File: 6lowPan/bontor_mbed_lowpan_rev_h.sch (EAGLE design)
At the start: 173 parts, among them IC1 SIM900, IC2 74HC595D, IC3 74HC595D, IC4 ADE7758RW, IC5 74HC595D, U2 W5500, X1 NX2520SA

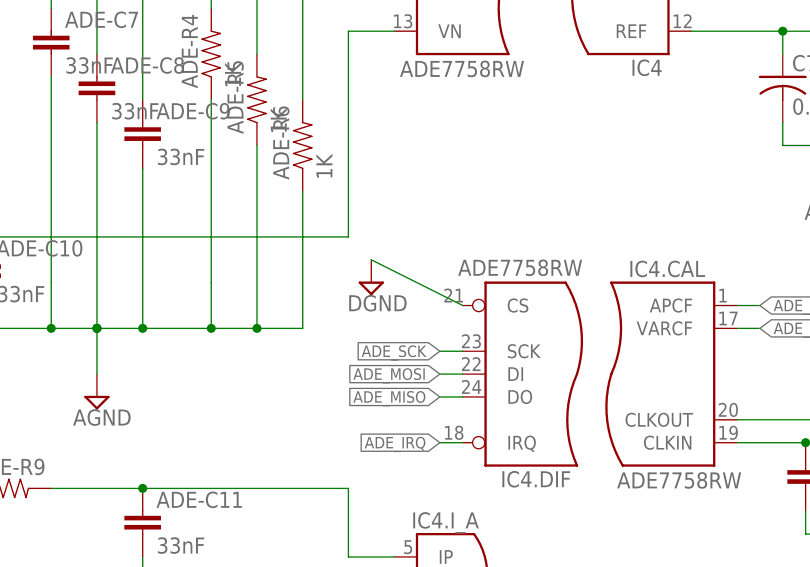
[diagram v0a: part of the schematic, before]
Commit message: add mcb enhancer BoM and gerber
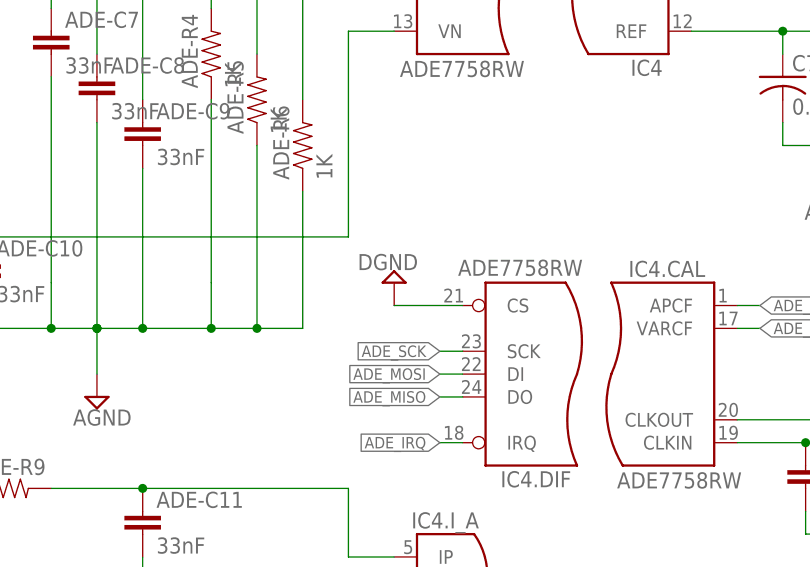
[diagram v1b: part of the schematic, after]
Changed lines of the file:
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@@
 <instance part="SUPPLY121" gate="G$1" x="622.3" y="119.38"/>
 <instance part="SUPPLY122" gate="G$1" x="546.1" y="25.4"/>
-<instance part="SUPPLY123" gate="G$1" x="299.72" y="144.78"/>
+<instance part="SUPPLY123" gate="G$1" x="302.26" y="144.78" rot="R180"/>
 <instance part="SUPPLY124" gate="G$1" x="502.92" y="106.68"/>
 <instance part="L1" gate="L" x="347.98" y="38.1" rot="R90"/>
@@
 <segment>
 <pinref part="IC4" gate=".DIF" pin="CS"/>
-<wire x1="309.88" y1="142.24" x2="299.72" y2="147.32" width="0.2032" layer="91"/>
+<wire x1="309.88" y1="142.24" x2="302.26" y2="142.24" width="0.2032" layer="91"/>
 <pinref part="SUPPLY123" gate="G$1" pin="DGND"/>
 </segment>

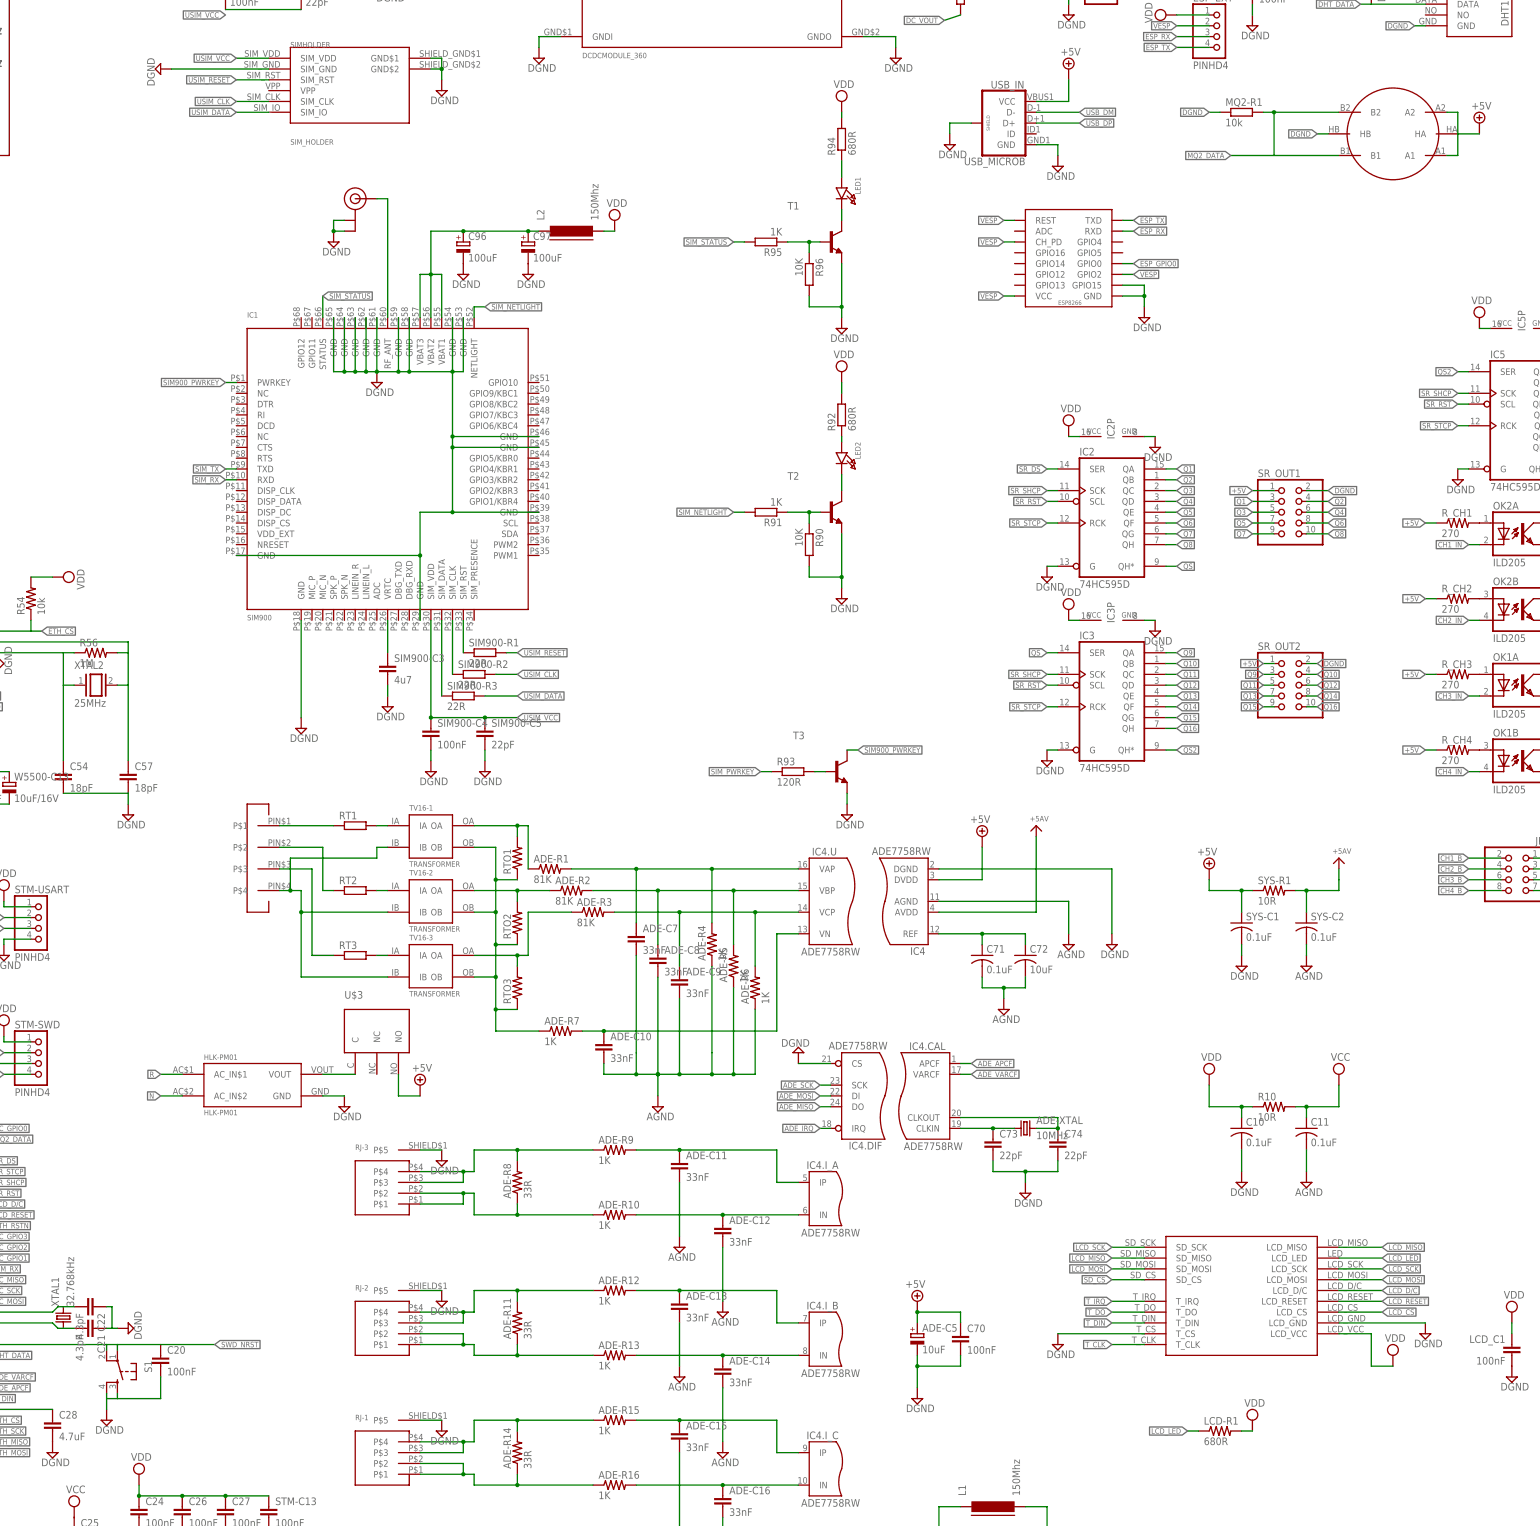
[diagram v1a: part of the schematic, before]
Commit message: added on off button and remove LCD resstor
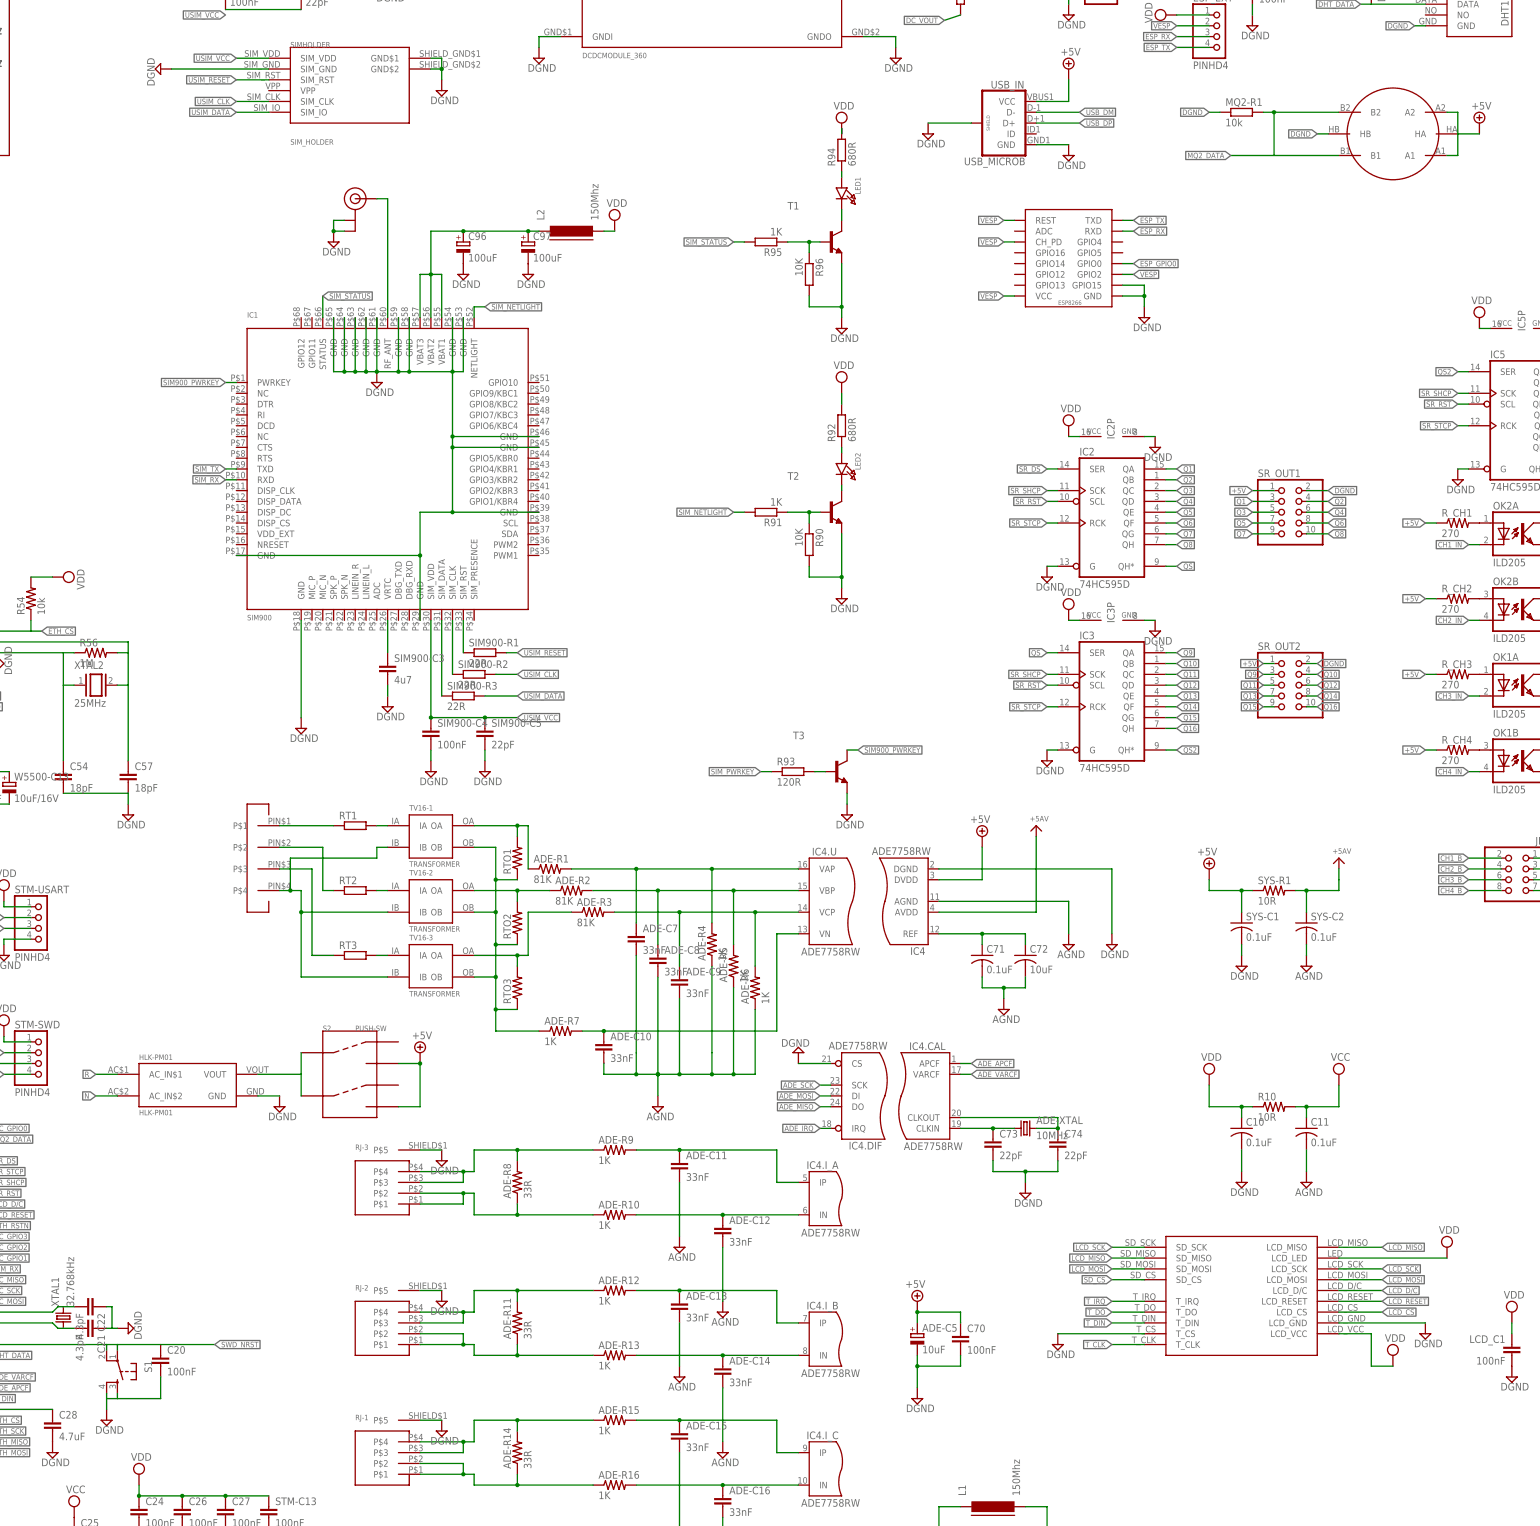
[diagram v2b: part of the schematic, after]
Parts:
- removed LCD-R1: 680R, SparkFun-Passives:RESISTOR0603-RES
- removed U$3: SW-KN1-102, bontor:SW-KN1-102
- added S2: PUSH-SW, Itead_BP_110825:SWITCH-6PIN-LOCK-2.54MM
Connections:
- removed net LCD_LED: LCD-R1.1, LCD14.LCD_LED
- net +5V: now also S2.P$3, S2.P$6; no longer U$3.NO
- net N$79: now also S2.P$1, S2.P$4; no longer U$3.C
- net VDD: now also LCD14.LCD_LED; no longer LCD-R1.2
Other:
- moved on the sheet: HLK-PM01, LED2, R92, R94
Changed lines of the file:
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@@
 <?xml version="1.0" encoding="utf-8"?>
 <!DOCTYPE eagle SYSTEM "eagle.dtd">
-<eagle version="6.3">
+<eagle version="7.2.0">
 <drawing>
 <settings>
@@
 <part name="ADE-R14" library="SparkFun-Passives" deviceset="RESISTOR" device="0402-RES" value="33R"/>
 <part name="SUPPLY72" library="supply2" deviceset="+5V" device=""/>
-<part name="LCD-R1" library="SparkFun-Passives" deviceset="RESISTOR" device="0603-RES" value="680R"/>
 <part name="SUPPLY81" library="supply2" deviceset="VDD" device=""/>
 <part name="SUPPLY84" library="supply2" deviceset="VDD" device=""/>
@@
 <part name="C28" library="rcl" deviceset="C-EU" device="C0603" value="4.7uF"/>
 <part name="SUPPLY131" library="supply2" deviceset="DGND" device=""/>
-<part name="U$3" library="bontor" deviceset="SW-KN1-102" device=""/>
+<part name="S2" library="Itead_BP_110825" deviceset="SWITCH-6PIN-LOCK-2.54MM" device="" value="PUSH-SW"/>
 </parts>
 <sheets>
@@
 <instance part="T1" gate="G$1" x="309.88" y="335.28"/>
 <instance part="LED1" gate="G$1" x="312.42" y="345.44" rot="R270"/>
-<instance part="R94" gate="G$1" x="312.42" y="359.41" rot="R90"/>
+<instance part="R94" gate="G$1" x="312.42" y="356.87" rot="R90"/>
 <instance part="R95" gate="G$1" x="294.64" y="335.28" rot="R180"/>
 <instance part="R96" gate="G$1" x="304.8" y="327.66" rot="R270"/>
 <instance part="T2" gate="G$1" x="309.88" y="271.78"/>
-<instance part="LED2" gate="G$1" x="312.42" y="283.21" rot="R270"/>
-<instance part="R92" gate="G$1" x="312.42" y="294.64" rot="R90"/>
+<instance part="LED2" gate="G$1" x="312.42" y="280.67" rot="R270"/>
+<instance part="R92" gate="G$1" x="312.42" y="292.1" rot="R90"/>
 <instance part="R91" gate="G$1" x="294.64" y="271.78" rot="R180"/>
 <instance part="R90" gate="G$1" x="304.8" y="264.16" rot="R270"/>
@@
 <instance part="SUPPLY106" gate="+5V" x="345.44" y="195.58" rot="MR0"/>
 <instance part="SUPPLY107" gate="+5V" x="398.78" y="187.96" rot="MR0"/>
-<instance part="SUPPLY109" gate="G$1" x="312.42" y="368.3"/>
-<instance part="SUPPLY110" gate="G$1" x="312.42" y="304.8"/>
+<instance part="SUPPLY109" gate="G$1" x="312.42" y="363.22"/>
+<instance part="SUPPLY110" gate="G$1" x="312.42" y="302.26"/>
 <instance part="SUPPLY112" gate="G$1" x="93.98" y="378.46" rot="R90"/>
 <instance part="ADE-R8" gate="G$1" x="236.22" y="114.3" rot="R90"/>
@@
 <instance part="ADE-R14" gate="G$1" x="236.22" y="50.8" rot="R90"/>
 <instance part="SUPPLY72" gate="+5V" x="330.2" y="86.36" rot="MR0"/>
-<instance part="LCD-R1" gate="G$1" x="401.32" y="55.88"/>
-<instance part="SUPPLY81" gate="G$1" x="408.94" y="58.42"/>
+<instance part="SUPPLY81" gate="G$1" x="454.66" y="99.06"/>
 <instance part="SUPPLY84" gate="G$1" x="365.76" y="292.1"/>
 <instance part="SUPPLY89" gate="G$1" x="365.76" y="248.92"/>
@@
 <instance part="USB_IN" gate="G$1" x="350.52" y="363.22" rot="MR0"/>
 <instance part="SUPPLY125" gate="+5V" x="365.76" y="375.92"/>
-<instance part="SUPPLY126" gate="G$1" x="363.22" y="353.06"/>
-<instance part="SUPPLY127" gate="G$1" x="337.82" y="358.14"/>
-<instance part="HLK-PM01" gate="G$1" x="162.56" y="132.08"/>
-<instance part="SUPPLY41" gate="+5V" x="213.36" y="137.16"/>
-<instance part="SUPPLY42" gate="G$1" x="195.58" y="132.08"/>
+<instance part="SUPPLY126" gate="G$1" x="365.76" y="355.6"/>
+<instance part="SUPPLY127" gate="G$1" x="332.74" y="360.68"/>
+<instance part="HLK-PM01" gate="G$1" x="147.32" y="132.08"/>
+<instance part="SUPPLY41" gate="+5V" x="213.36" y="144.78"/>
+<instance part="SUPPLY42" gate="G$1" x="180.34" y="132.08"/>
 <instance part="DCDC" gate="G$1" x="281.94" y="391.16"/>
 <instance part="RJ-3" gate="G$1" x="198.12" y="106.68"/>
@@
 <instance part="C28" gate="G$1" x="127" y="58.42"/>
 <instance part="SUPPLY131" gate="G$1" x="127" y="50.8"/>
-<instance part="U$3" gate="G$1" x="203.2" y="149.86"/>
+<instance part="S2" gate="G$1" x="195.58" y="139.7"/>
 </instances>
 <busses>
@@
 <pinref part="USB_IN" gate="G$1" pin="GND"/>
 <pinref part="SUPPLY126" gate="G$1" pin="DGND"/>
-<wire x1="358.14" y1="358.14" x2="363.22" y2="358.14" width="0.1524" layer="91"/>
-<wire x1="363.22" y1="358.14" x2="363.22" y2="355.6" width="0.1524" layer="91"/>
+<wire x1="358.14" y1="358.14" x2="365.76" y2="358.14" width="0.1524" layer="91"/>
 </segment>
 <segment>
 <pinref part="USB_IN" gate="G$1" pin="SHIELD"/>
 <pinref part="SUPPLY127" gate="G$1" pin="DGND"/>
-<wire x1="342.9" y1="363.22" x2="337.82" y2="363.22" width="0.1524" layer="91"/>
-<wire x1="337.82" y1="363.22" x2="337.82" y2="360.68" width="0.1524" layer="91"/>
+<wire x1="342.9" y1="363.22" x2="332.74" y2="363.22" width="0.1524" layer="91"/>
 </segment>
 <segment>
 <pinref part="HLK-PM01" gate="G$1" pin="GND"/>
-<wire x1="190.5" y1="134.62" x2="195.58" y2="134.62" width="0.1524" layer="91"/>
+<wire x1="175.26" y1="134.62" x2="180.34" y2="134.62" width="0.1524" layer="91"/>
 <pinref part="SUPPLY42" gate="G$1" pin="DGND"/>
 </segment>
@@
 <segment>
 <pinref part="R94" gate="G$1" pin="2"/>
-<wire x1="312.42" y1="364.49" x2="312.42" y2="365.76" width="0.1524" layer="91"/>
+<wire x1="312.42" y1="361.95" x2="312.42" y2="360.68" width="0.1524" layer="91"/>
 <pinref part="SUPPLY109" gate="G$1" pin="VDD"/>
 </segment>
@@
 <pinref part="R92" gate="G$1" pin="2"/>
 <pinref part="SUPPLY110" gate="G$1" pin="VDD"/>
-<wire x1="312.42" y1="302.26" x2="312.42" y2="299.72" width="0.1524" layer="91"/>
+<wire x1="312.42" y1="299.72" x2="312.42" y2="297.18" width="0.1524" layer="91"/>
 </segment>
 <segment>
@@
 </segment>
 <segment>
-<pinref part="LCD-R1" gate="G$1" pin="2"/>
-<pinref part="SUPPLY81" gate="G$1" pin="VDD"/>
-<wire x1="408.94" y1="55.88" x2="406.4" y2="55.88" width="0.1524" layer="91"/>
-</segment>
-<segment>
 <pinref part="IC3" gate="P" pin="VCC"/>
 <pinref part="SUPPLY89" gate="G$1" pin="VDD"/>
@@
 <wire x1="469.9" y1="78.74" x2="469.9" y2="81.28" width="0.1524" layer="91"/>
 </segment>
+<segment>
+<wire x1="429.26" y1="96.52" x2="454.66" y2="96.52" width="0.1524" layer="91"/>
+<pinref part="LCD14" gate="G$1" pin="LCD_LED"/>
+<pinref part="SUPPLY81" gate="G$1" pin="VDD"/>
+</segment>
 </net>
 <net name="SWD_NRST" class="0">
@@
 </segment>
 <segment>
+<pinref part="S2" gate="G$1" pin="P$3"/>
+<wire x1="208.28" y1="142.24" x2="213.36" y2="142.24" width="0.1524" layer="91"/>
+<wire x1="213.36" y1="142.24" x2="213.36" y2="132.08" width="0.1524" layer="91"/>
+<pinref part="S2" gate="G$1" pin="P$6"/>
+<wire x1="213.36" y1="132.08" x2="208.28" y2="132.08" width="0.1524" layer="91"/>
 <pinref part="SUPPLY41" gate="+5V" pin="+5V"/>
-<wire x1="208.28" y1="134.62" x2="213.36" y2="134.62" width="0.1524" layer="91"/>
-<pinref part="U$3" gate="G$1" pin="NO"/>
-<wire x1="208.28" y1="139.7" x2="208.28" y2="134.62" width="0.1524" layer="91"/>
+<junction x="213.36" y="142.24"/>
 </segment>
 </net>
@@
 <pinref part="LED1" gate="G$1" pin="A"/>
 <pinref part="R94" gate="G$1" pin="1"/>
-<wire x1="312.42" y1="354.33" x2="312.42" y2="350.52" width="0.1524" layer="91"/>
+<wire x1="312.42" y1="351.79" x2="312.42" y2="350.52" width="0.1524" layer="91"/>
 </segment>
 </net>
@@
 <pinref part="LED2" gate="G$1" pin="A"/>
 <pinref part="R92" gate="G$1" pin="1"/>
-<wire x1="312.42" y1="289.56" x2="312.42" y2="288.29" width="0.1524" layer="91"/>
+<wire x1="312.42" y1="287.02" x2="312.42" y2="285.75" width="0.1524" layer="91"/>
 </segment>
 </net>
@@
 <pinref part="LED2" gate="G$1" pin="C"/>
 <pinref part="T2" gate="G$1" pin="C"/>
-<wire x1="312.42" y1="276.86" x2="312.42" y2="280.67" width="0.1524" layer="91"/>
+<wire x1="312.42" y1="276.86" x2="312.42" y2="278.13" width="0.1524" layer="91"/>
 </segment>
 </net>
@@
 </segment>
 </net>
-<net name="LCD_LED" class="0">
-<segment>
-<pinref part="LCD-R1" gate="G$1" pin="1"/>
-<wire x1="396.24" y1="55.88" x2="393.7" y2="55.88" width="0.1524" layer="91"/>
-<label x="393.7" y="55.88" size="1.27" layer="95" rot="R180" xref="yes"/>
-</segment>
-<segment>
-<wire x1="429.26" y1="96.52" x2="439.42" y2="96.52" width="0.1524" layer="91"/>
-<label x="439.42" y="96.52" size="1.27" layer="95" xref="yes"/>
-<pinref part="LCD14" gate="G$1" pin="LCD_LED"/>
-</segment>
-</net>
 <net name="LCD_D/C" class="0">
 <segment>
@@
 <segment>
 <pinref part="HLK-PM01" gate="G$1" pin="AC_IN$2"/>
-<wire x1="157.48" y1="134.62" x2="152.4" y2="134.62" width="0.1524" layer="91"/>
-<label x="152.4" y="134.62" size="1.27" layer="95" ratio="5" rot="R180" xref="yes"/>
+<wire x1="142.24" y1="134.62" x2="137.16" y2="134.62" width="0.1524" layer="91"/>
+<label x="137.16" y="134.62" size="1.27" layer="95" ratio="5" rot="R180" xref="yes"/>
 </segment>
 </net>
@@
 <segment>
 <pinref part="HLK-PM01" gate="G$1" pin="AC_IN$1"/>
-<wire x1="157.48" y1="139.7" x2="152.4" y2="139.7" width="0.1524" layer="91"/>
-<label x="152.4" y="139.7" size="1.27" layer="95" ratio="5" rot="R180" xref="yes"/>
+<wire x1="142.24" y1="139.7" x2="137.16" y2="139.7" width="0.1524" layer="91"/>
+<label x="137.16" y="139.7" size="1.27" layer="95" ratio="5" rot="R180" xref="yes"/>
 </segment>
 </net>
@@
 <segment>
 <pinref part="HLK-PM01" gate="G$1" pin="VOUT"/>
-<pinref part="U$3" gate="G$1" pin="C"/>
-<wire x1="190.5" y1="139.7" x2="198.12" y2="139.7" width="0.1524" layer="91"/>
+<wire x1="175.26" y1="139.7" x2="185.42" y2="139.7" width="0.1524" layer="91"/>
+<pinref part="S2" gate="G$1" pin="P$1"/>
+<wire x1="185.42" y1="139.7" x2="185.42" y2="144.78" width="0.1524" layer="91"/>
+<pinref part="S2" gate="G$1" pin="P$4"/>
+<wire x1="185.42" y1="134.62" x2="185.42" y2="139.7" width="0.1524" layer="91"/>
 </segment>
 </net>
